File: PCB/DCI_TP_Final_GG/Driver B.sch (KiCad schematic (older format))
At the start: 18 parts

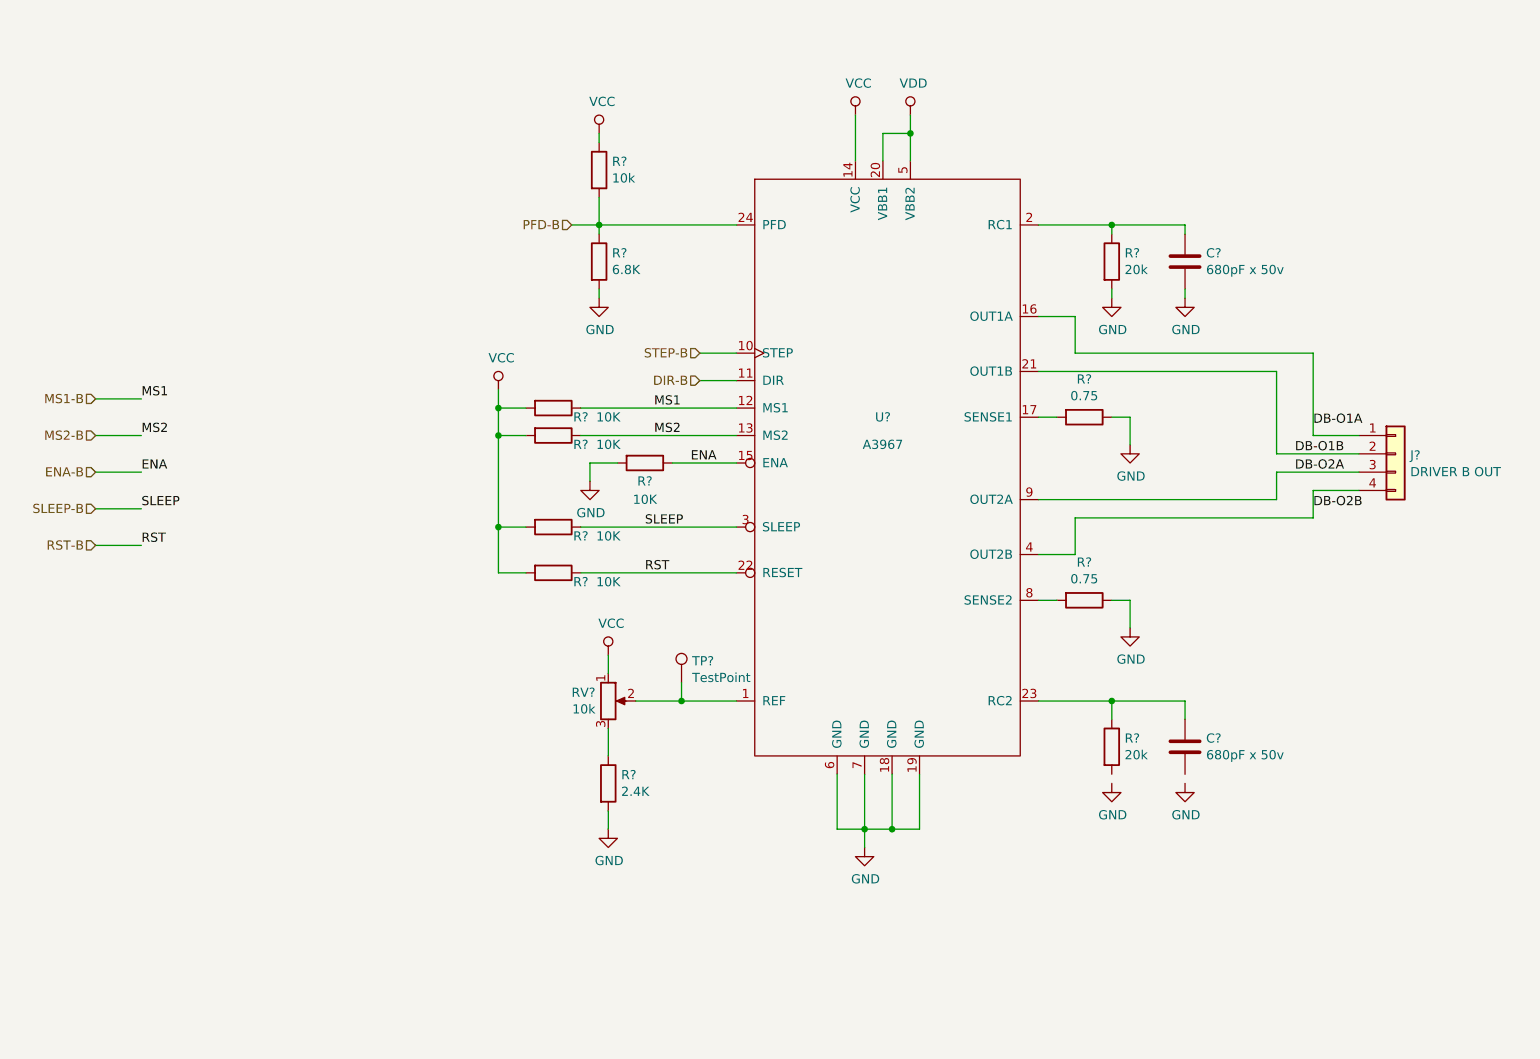
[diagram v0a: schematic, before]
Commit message: Hoja de fuente y conectores completa.
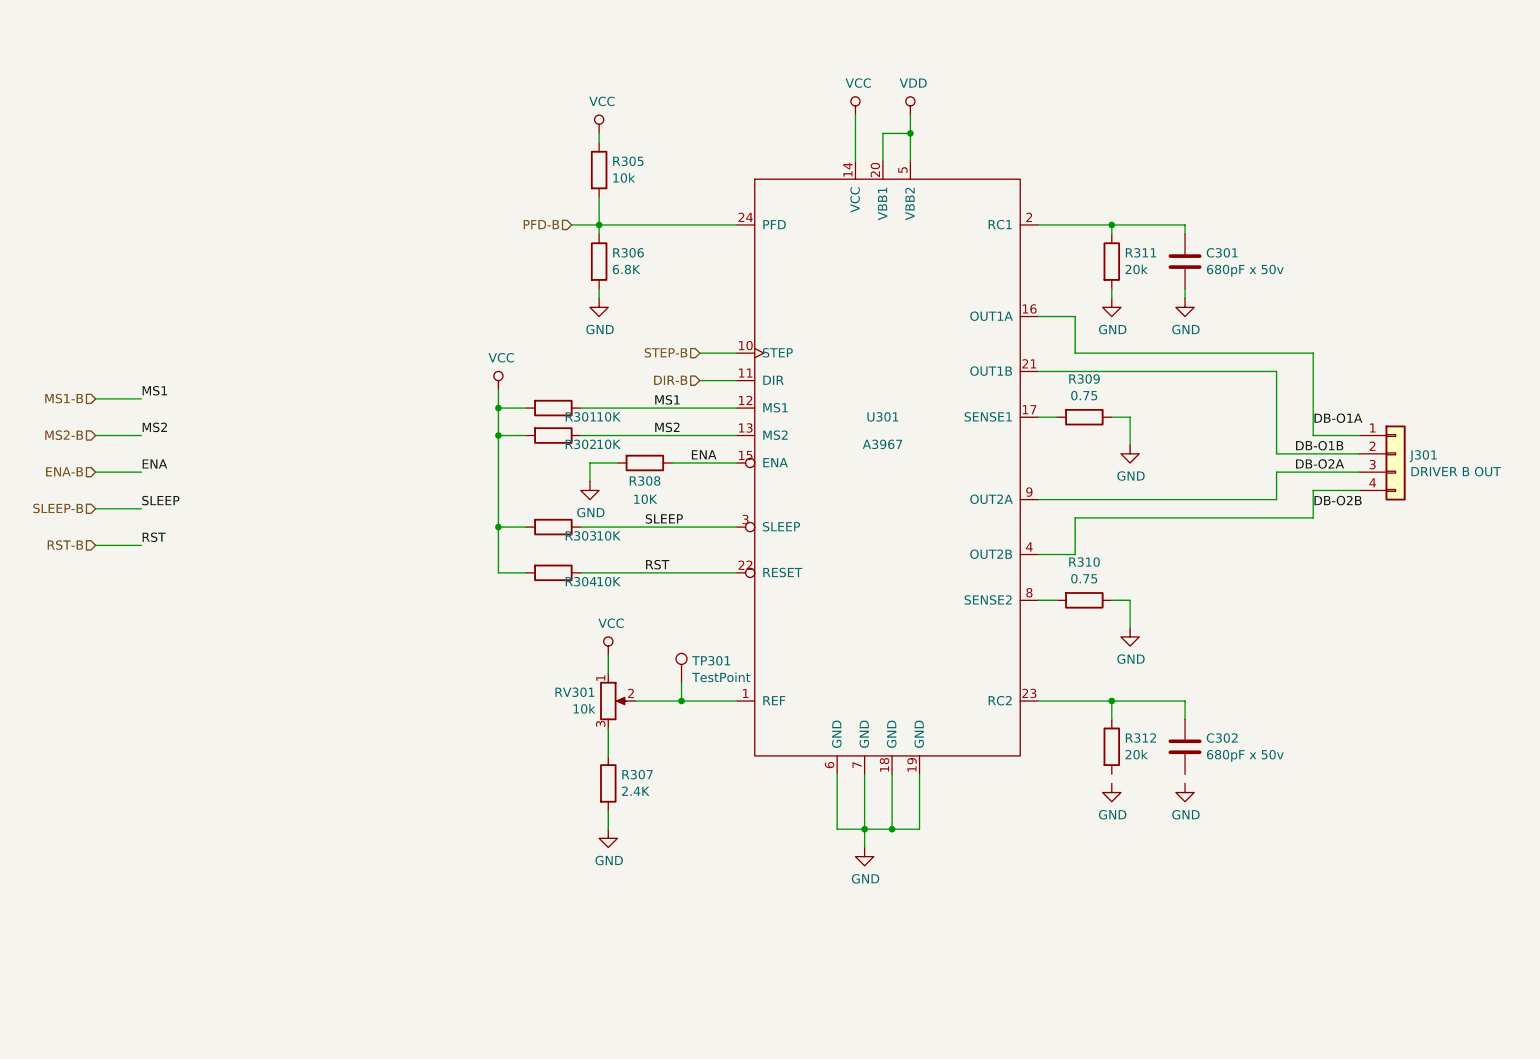
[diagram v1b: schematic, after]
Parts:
- TP301: renamed from TP?; footprint (none) -> TestPoint:TestPoint_Pad_D2.0mm
- gave numbers to parts that had none: 17

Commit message: Se completo el esquematico y documentación. El esquematico esta listo para una primera revisión.
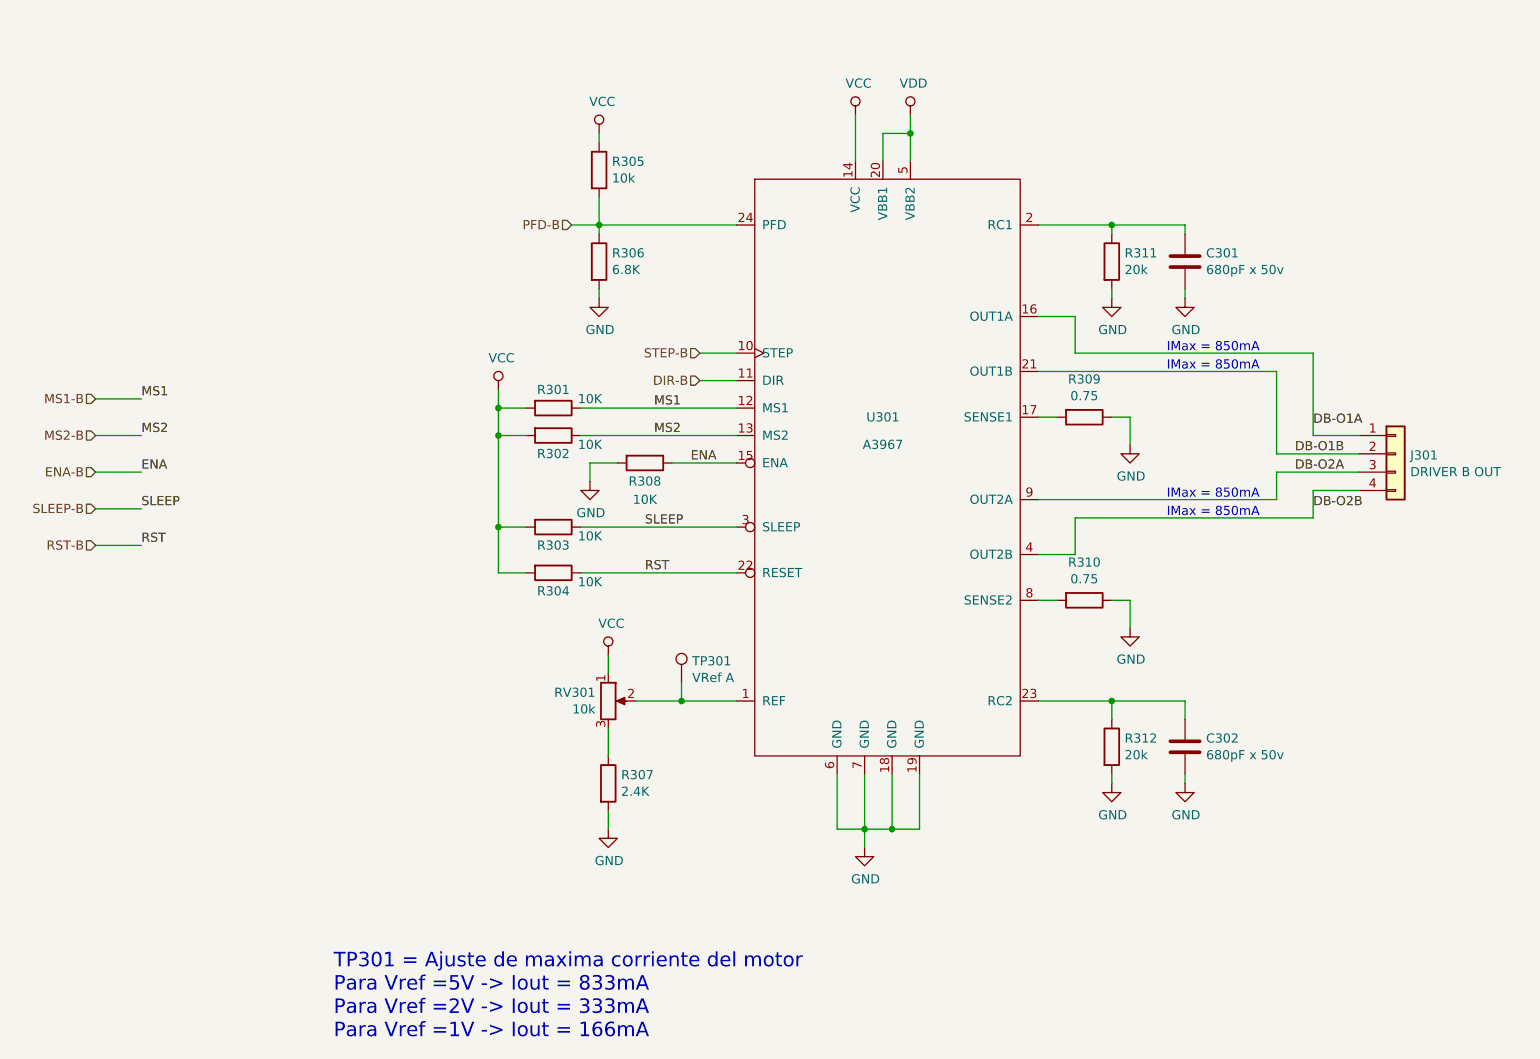
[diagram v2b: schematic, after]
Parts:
- TP301: value TestPoint -> VRef A
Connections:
- net GND: now also C302.2, R312.2
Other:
- note added: "IMax = 850mA"
- note added: "TP301 = Ajuste de maxima corriente del motor\nPara Vref =5V -> Iout = 833mA\nPara Vref =2V -> Iout = 333mA\nPara Vref =1V -> Iout = 166mA"
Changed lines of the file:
@@
 AR Path="/5D9739FA/5DA0DA46" Ref="TP301"  Part="1"
 F 0 "TP301" H 5308 4818 50  0000 L CNN
-F 1 "TestPoint" H 5308 4727 50  0000 L CNN
+F 1 "VRef A" H 5308 4727 50  0000 L CNN
 F 2 "TestPoint:TestPoint_Pad_D2.0mm" H 5450 4700 50  0001 C CNN
 F 3 "" H 5450 4700 50  0001 C CNN
@@
 AR Path="/5D9739A6/5DA0DA61" Ref="R?"  Part="1"
 AR Path="/5D9739FA/5DA0DA61" Ref="R302"  Part="1"
-F 0 "R302" V 4600 3500 50  0000 C CNN
-F 1 "10K" V 4600 3650 50  0000 C CNN
+F 0 "R302" V 4650 3350 50  0000 C CNN
+F 1 "10K" V 4600 3550 50  0000 C CNN
 F 2 "Resistor_SMD:R_0805_2012Metric" V 4480 3350 50  0001 C CNN
 F 3 "" H 4550 3350 50  0001 C CNN
@@
 AR Path="/5D9739A6/5DA0DA67" Ref="R?"  Part="1"
 AR Path="/5D9739FA/5DA0DA67" Ref="R301"  Part="1"
-F 0 "R301" V 4600 3350 50  0000 C CNN
-F 1 "10K" V 4600 3500 50  0000 C CNN
+F 0 "R301" V 4450 3200 50  0000 C CNN
+F 1 "10K" V 4500 3400 50  0000 C CNN
 F 2 "Resistor_SMD:R_0805_2012Metric" V 4480 3200 50  0001 C CNN
 F 3 "" H 4550 3200 50  0001 C CNN
@@
 AR Path="/5D9739A6/5DA0DA6F" Ref="R?"  Part="1"
 AR Path="/5D9739FA/5DA0DA6F" Ref="R303"  Part="1"
-F 0 "R303" V 4600 4000 50  0000 C CNN
-F 1 "10K" V 4600 4150 50  0000 C CNN
+F 0 "R303" V 4650 3850 50  0000 C CNN
+F 1 "10K" V 4600 4050 50  0000 C CNN
 F 2 "Resistor_SMD:R_0805_2012Metric" V 4480 3850 50  0001 C CNN
 F 3 "" H 4550 3850 50  0001 C CNN
@@
 AR Path="/5D9739A6/5DA0DA75" Ref="R?"  Part="1"
 AR Path="/5D9739FA/5DA0DA75" Ref="R304"  Part="1"
-F 0 "R304" V 4600 4250 50  0000 C CNN
-F 1 "10K" V 4600 4400 50  0000 C CNN
+F 0 "R304" V 4650 4100 50  0000 C CNN
+F 1 "10K" V 4600 4300 50  0000 C CNN
 F 2 "Resistor_SMD:R_0805_2012Metric" V 4480 4100 50  0001 C CNN
 F 3 "" H 4550 4100 50  0001 C CNN
@@
 Text Label 8700 3750 0    50   ~ 0
 DB-O2B
+Wire Wire Line
+	8000 5200 8000 5250
+Wire Wire Line
+	7600 5200 7600 5250
+Text Notes 7900 2900 0    50   ~ 0
+IMax = 850mA
+Text Notes 7900 3000 0    50   ~ 0
+IMax = 850mA
+Text Notes 7900 3700 0    50   ~ 0
+IMax = 850mA
+Text Notes 7900 3800 0    50   ~ 0
+IMax = 850mA
+Text Notes 3350 6650 0    79   ~ 0
+TP301 = Ajuste de maxima corriente del motor\nPara Vref =5V -> Iout = 833mA\nPara Vref =2V -> Iout = 333mA\nPara Vref =1V -> Iout = 166mA
 $EndSCHEMATC

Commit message: Inicio etapa de desarrollo de PCB, agrego biblioteca de borneras
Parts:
- J301: footprint TerminalBlock:TerminalBlock_Altech_AK300-4_P5.00mm -> TerminalBlock_Phoenix:TerminalBlock_Phoenix_MKDS-1,5-4_1x04_P5.00mm_Horizontal
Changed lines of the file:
@@
 F 0 "J301" H 9230 3442 50  0000 L CNN
 F 1 "DRIVER B OUT" H 9230 3351 50  0000 L CNN
-F 2 "TerminalBlock:TerminalBlock_Altech_AK300-4_P5.00mm" H 9150 3450 50  0001 C CNN
+F 2 "TerminalBlock_Phoenix:TerminalBlock_Phoenix_MKDS-1,5-4_1x04_P5.00mm_Horizontal" H 9150 3450 50  0001 C CNN
 F 3 "" H 9150 3450 50  0001 C CNN
 	1    9150 3450

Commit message: Agrego 3D de borneras
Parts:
- RV301: #Fab (none) -> TS53YJ103MR10; Digikey (none) -> TS53YJ-10KTR-ND
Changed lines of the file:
@@
 F 2 "Potentiometer_SMD:Potentiometer_Vishay_TS53YJ_Vertical" H 4850 4800 50  0001 C CNN
 F 3 "" H 4850 4800 50  0001 C CNN
+F 4 "TS53YJ-10KTR-ND" H 4850 4800 50  0001 C CNN "Digikey"
+F 5 "TS53YJ103MR10" H 4850 4800 50  0001 C CNN "#Fab"
 	1    4850 4800
 	1    0    0    -1

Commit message: Agrego codigos de catalogo
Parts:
- C301, C302: Descripcion CAP 680PF 50V CERAMICO 0805 -> CAP CER 680PF 50V; digikey# (none) -> 399-8110-1-ND; manf (none) -> KEMET; manf# (none) -> C681F5GACTU
- J301: Descripcion (none) -> Terminal Block x 4 5MM PCB; digikey# (none) -> 277-1238-ND; manf (none) -> Phoenix Contact; manf# (none) -> 1729034
- R301, R302, R303, R304, R308: Descripcion (none) -> RES 10K OHM SMD 0805; digikey# (none) -> 311-10KARCT-ND; manf (none) -> Yageo; manf# (none) -> RC0805JR-0710KL
- R305: digikey# (none) -> 311-10KARCT-ND; manf (none) -> Yageo; manf# (none) -> RC0805JR-0710KL
- R306: Descripcion RES SMD 6.8K OHM 0805 -> RES 6.8K OHM SMD 0805; digikey# (none) -> 311-6.80KCRCT-ND; manf (none) -> Yageo; manf# (none) -> RC0805FR-076K8L
- R307: digikey# (none) -> 311-2.40KCRCT-ND; manf (none) -> Yageo; manf# (none) -> RC0805FR-072K4L
- R309: Descripcion Resistencia SMD 0805 1/4 w 1% -> RES .75 OHM 1/4W 1% 0805 SMD; digikey# (none) -> RCWE.75DCT-ND; manf (none) -> Vishay Dale; manf# (none) -> RCWE0805R750FKEA
- R310: digikey# (none) -> RCWE.75DCT-ND; manf (none) -> Vishay Dale; manf# (none) -> RCWE0805R750FKEA
- R311, R312: Descripcion RES 20K OHM 0805 -> RES 20K OHM SMD 0805; digikey# (none) -> 311-20.0KCRCT-ND; manf (none) -> Yageo; manf# (none) -> RC0805FR-0720KL
- RV301: #Fab TS53YJ103MR10 -> (none); Descripcion (none) -> Potenciometro 10k SMD 5050; Digikey TS53YJ-10KTR-ND -> (none); digikey# (none) -> TS53YJ-10KTR-ND; manf (none) -> Vishay; manf# (none) -> TS53YJ103MR10
- U301: Descripcion (none) -> Stepper Driver A3967; digikey# (none) -> 620-1140-1-ND; manf (none) -> Allegro MicroSystems; manf# (none) -> A3967SLBTR-T
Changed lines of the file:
@@
 Title "Replica Dual EasyDriver v4.5"
 Date "2019-10-02"
-Rev ""
+Rev "Matias Brignone"
 Comp "Gonzalo Gontad - CESE-FIUBA"
 Comment1 ""
@@
 F 2 "Package_SO:SOIC-24W_7.5x15.4mm_P1.27mm" V 6650 -1450 50  0001 C CNN
 F 3 "https://github.com/cese-dci/tp-dci--Gonzalogontad/blob/master/info/A3967-Datasheet.pdf" H 6350 -1300 50  0001 C CNN
+F 4 "Stepper Driver A3967" H 3800 1000 50  0001 C CNN "Descripcion"
+F 5 "620-1140-1-ND" H 3800 1000 50  0001 C CNN "digikey#"
+F 6 "Allegro MicroSystems" H 3800 1000 50  0001 C CNN "manf"
+F 7 "A3967SLBTR-T" H 3800 1000 50  0001 C CNN "manf#"
 	1    3800 1000
 	1    0    0    -1
@@
 F 2 "TerminalBlock_Phoenix:TerminalBlock_Phoenix_MKDS-1,5-4_1x04_P5.00mm_Horizontal" H 9150 3450 50  0001 C CNN
 F 3 "" H 9150 3450 50  0001 C CNN
+F 4 "Terminal Block x 4  5MM PCB" H 9150 3450 50  0001 C CNN "Descripcion"
+F 5 "277-1238-ND" H 9150 3450 50  0001 C CNN "digikey#"
+F 6 "Phoenix Contact" H 9150 3450 50  0001 C CNN "manf"
+F 7 "1729034" H 9150 3450 50  0001 C CNN "manf#"
 	1    9150 3450
 	1    0    0    -1
@@
 F 2 "Resistor_SMD:R_0805_2012Metric" V 7380 3250 50  0001 C CNN
 F 3 "" H 7450 3250 50  0001 C CNN
-F 4 "Resistencia SMD 0805 1/4 w 1%" V 7450 3250 50  0001 C CNN "Descripcion"
+F 4 "RES .75 OHM 1/4W 1% 0805 SMD" V 7450 3250 50  0001 C CNN "Descripcion"
+F 5 "RCWE.75DCT-ND" H 7450 3250 50  0001 C CNN "digikey#"
+F 6 "Vishay Dale" H 7450 3250 50  0001 C CNN "manf"
+F 7 "RCWE0805R750FKEA" H 7450 3250 50  0001 C CNN "manf#"
 	1    7450 3250
 	0    1    1    0
@@
 F 3 "" H 7450 4250 50  0001 C CNN
 F 4 "RES .75 OHM 1/4W 1% 0805 SMD" V 7450 4250 50  0001 C CNN "Descripcion"
+F 5 "RCWE.75DCT-ND" H 7450 4250 50  0001 C CNN "digikey#"
+F 6 "Vishay Dale" H 7450 4250 50  0001 C CNN "manf"
+F 7 "RCWE0805R750FKEA" H 7450 4250 50  0001 C CNN "manf#"
 	1    7450 4250
 	0    1    1    0
@@
 F 2 "Resistor_SMD:R_0805_2012Metric" V 7530 5050 50  0001 C CNN
 F 3 "" H 7600 5050 50  0001 C CNN
-F 4 "RES 20K OHM 0805" H 7600 5050 50  0001 C CNN "Descripcion"
+F 4 "RES 20K OHM SMD 0805" H 7600 5050 50  0001 C CNN "Descripcion"
+F 5 "311-20.0KCRCT-ND" H 7600 5050 50  0001 C CNN "digikey#"
+F 6 "Yageo" H 7600 5050 50  0001 C CNN "manf"
+F 7 "RC0805FR-0720KL" H 7600 5050 50  0001 C CNN "manf#"
 	1    7600 5050
 	1    0    0    -1
@@
 F 2 "Capacitor_SMD:C_0805_2012Metric" H 8038 4900 50  0001 C CNN
 F 3 "" H 8000 5050 50  0001 C CNN
-F 4 "CAP 680PF 50V CERAMICO 0805" H 8000 5050 50  0001 C CNN "Descripcion"
+F 4 "CAP CER 680PF 50V " H 8000 5050 50  0001 C CNN "Descripcion"
+F 5 "399-8110-1-ND" H 8000 5050 50  0001 C CNN "digikey#"
+F 6 "KEMET" H 8000 5050 50  0001 C CNN "manf"
+F 7 "C681F5GACTU" H 8000 5050 50  0001 C CNN "manf#"
 	1    8000 5050
 	1    0    0    -1
@@
 F 2 "Resistor_SMD:R_0805_2012Metric" V 7530 2400 50  0001 C CNN
 F 3 "" H 7600 2400 50  0001 C CNN
-F 4 "RES 20K OHM 0805" H 7600 2400 50  0001 C CNN "Descripcion"
+F 4 "RES 20K OHM SMD 0805" H 7600 2400 50  0001 C CNN "Descripcion"
+F 5 "311-20.0KCRCT-ND" H 7600 2400 50  0001 C CNN "digikey#"
+F 6 "Yageo" H 7600 2400 50  0001 C CNN "manf"
+F 7 "RC0805FR-0720KL" H 7600 2400 50  0001 C CNN "manf#"
 	1    7600 2400
 	1    0    0    -1
@@
 F 2 "Capacitor_SMD:C_0805_2012Metric" H 8038 2250 50  0001 C CNN
 F 3 "" H 8000 2400 50  0001 C CNN
-F 4 "CAP 680PF 50V CERAMICO 0805" H 8000 2400 50  0001 C CNN "Descripcion"
+F 4 "CAP CER 680PF 50V " H 8000 2400 50  0001 C CNN "Descripcion"
+F 5 "399-8110-1-ND" H 8000 2400 50  0001 C CNN "digikey#"
+F 6 "KEMET" H 8000 2400 50  0001 C CNN "manf"
+F 7 "C681F5GACTU" H 8000 2400 50  0001 C CNN "manf#"
 	1    8000 2400
 	1    0    0    -1
@@
 F 2 "Resistor_SMD:R_0805_2012Metric" V 4730 2400 50  0001 C CNN
 F 3 "" H 4800 2400 50  0001 C CNN
-F 4 "RES SMD 6.8K OHM 0805" H 4800 2400 50  0001 C CNN "Descripcion"
+F 4 "RES  6.8K OHM SMD 0805" H 4800 2400 50  0001 C CNN "Descripcion"
+F 5 "311-6.80KCRCT-ND" H 4800 2400 50  0001 C CNN "digikey#"
+F 6 "Yageo" H 4800 2400 50  0001 C CNN "manf"
+F 7 "RC0805FR-076K8L" H 4800 2400 50  0001 C CNN "manf#"
 	1    4800 2400
 	1    0    0    -1
@@
 F 3 "" H 4800 1900 50  0001 C CNN
 F 4 "RES 10K OHM SMD 0805" H 4800 1900 50  0001 C CNN "Descripcion"
+F 5 "311-10KARCT-ND" H 4800 1900 50  0001 C CNN "digikey#"
+F 6 "Yageo" H 4800 1900 50  0001 C CNN "manf"
+F 7 "RC0805JR-0710KL" H 4800 1900 50  0001 C CNN "manf#"
 	1    4800 1900
 	1    0    0    -1
@@
 F 2 "Potentiometer_SMD:Potentiometer_Vishay_TS53YJ_Vertical" H 4850 4800 50  0001 C CNN
 F 3 "" H 4850 4800 50  0001 C CNN
-F 4 "TS53YJ-10KTR-ND" H 4850 4800 50  0001 C CNN "Digikey"
-F 5 "TS53YJ103MR10" H 4850 4800 50  0001 C CNN "#Fab"
+F 4 "TS53YJ-10KTR-ND" H 4850 4800 50  0001 C CNN "digikey#"
+F 5 "TS53YJ103MR10" H 4850 4800 50  0001 C CNN "manf#"
+F 6 "Potenciometro 10k SMD 5050" H 4850 4800 50  0001 C CNN "Descripcion"
+F 7 "Vishay" H 4850 4800 50  0001 C CNN "manf"
 	1    4850 4800
 	1    0    0    -1
@@
 F 3 "" H 4850 5250 50  0001 C CNN
 F 4 "RES 2.4K OHM SMD 0805" H 4850 5250 50  0001 C CNN "Descripcion"
+F 5 "311-2.40KCRCT-ND" H 4850 5250 50  0001 C CNN "digikey#"
+F 6 "Yageo" H 4850 5250 50  0001 C CNN "manf"
+F 7 "RC0805FR-072K4L" H 4850 5250 50  0001 C CNN "manf#"
 	1    4850 5250
 	1    0    0    -1
@@
 F 2 "Resistor_SMD:R_0805_2012Metric" V 4980 3500 50  0001 C CNN
 F 3 "" H 5050 3500 50  0001 C CNN
+F 4 "RES 10K OHM SMD 0805" H 5050 3500 50  0001 C CNN "Descripcion"
+F 5 "311-10KARCT-ND" H 5050 3500 50  0001 C CNN "digikey#"
+F 6 "Yageo" H 5050 3500 50  0001 C CNN "manf"
+F 7 "RC0805JR-0710KL" H 5050 3500 50  0001 C CNN "manf#"
 	1    5050 3500
 	0    1    1    0
@@
 F 2 "Resistor_SMD:R_0805_2012Metric" V 4480 3350 50  0001 C CNN
 F 3 "" H 4550 3350 50  0001 C CNN
+F 4 "RES 10K OHM SMD 0805" H 4550 3350 50  0001 C CNN "Descripcion"
+F 5 "311-10KARCT-ND" H 4550 3350 50  0001 C CNN "digikey#"
+F 6 "Yageo" H 4550 3350 50  0001 C CNN "manf"
+F 7 "RC0805JR-0710KL" H 4550 3350 50  0001 C CNN "manf#"
 	1    4550 3350
 	0    1    1    0
@@
 F 2 "Resistor_SMD:R_0805_2012Metric" V 4480 3200 50  0001 C CNN
 F 3 "" H 4550 3200 50  0001 C CNN
+F 4 "RES 10K OHM SMD 0805" H 4550 3200 50  0001 C CNN "Descripcion"
+F 5 "311-10KARCT-ND" H 4550 3200 50  0001 C CNN "digikey#"
+F 6 "Yageo" H 4550 3200 50  0001 C CNN "manf"
+F 7 "RC0805JR-0710KL" H 4550 3200 50  0001 C CNN "manf#"
 	1    4550 3200
 	0    1    1    0
@@
 F 2 "Resistor_SMD:R_0805_2012Metric" V 4480 3850 50  0001 C CNN
 F 3 "" H 4550 3850 50  0001 C CNN
+F 4 "RES 10K OHM SMD 0805" H 4550 3850 50  0001 C CNN "Descripcion"
+F 5 "311-10KARCT-ND" H 4550 3850 50  0001 C CNN "digikey#"
+F 6 "Yageo" H 4550 3850 50  0001 C CNN "manf"
+F 7 "RC0805JR-0710KL" H 4550 3850 50  0001 C CNN "manf#"
 	1    4550 3850
 	0    1    1    0
@@
 F 2 "Resistor_SMD:R_0805_2012Metric" V 4480 4100 50  0001 C CNN
 F 3 "" H 4550 4100 50  0001 C CNN
+F 4 "RES 10K OHM SMD 0805" H 4550 4100 50  0001 C CNN "Descripcion"
+F 5 "311-10KARCT-ND" H 4550 4100 50  0001 C CNN "digikey#"
+F 6 "Yageo" H 4550 4100 50  0001 C CNN "manf"
+F 7 "RC0805JR-0710KL" H 4550 4100 50  0001 C CNN "manf#"
 	1    4550 4100
 	0    1    1    0
